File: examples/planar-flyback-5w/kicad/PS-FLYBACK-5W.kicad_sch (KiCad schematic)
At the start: 26 parts, among them J1 18-36 V DC, J2 5 V / 1 A isolated, T1 PLANAR 4:2 / Lm 12uH, U1 LT8302ES8E#PBF

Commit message: Use American Embedded M3 Edge mounting footprints
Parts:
- H1, H2, H3, H4: footprint amemb-MountingHole:MountingHole_3.2mm_M3_ExposedSubstrate -> amemb-MountingHole:MountingHole_3.2mm_M3_ExposedSubstrate_Edge

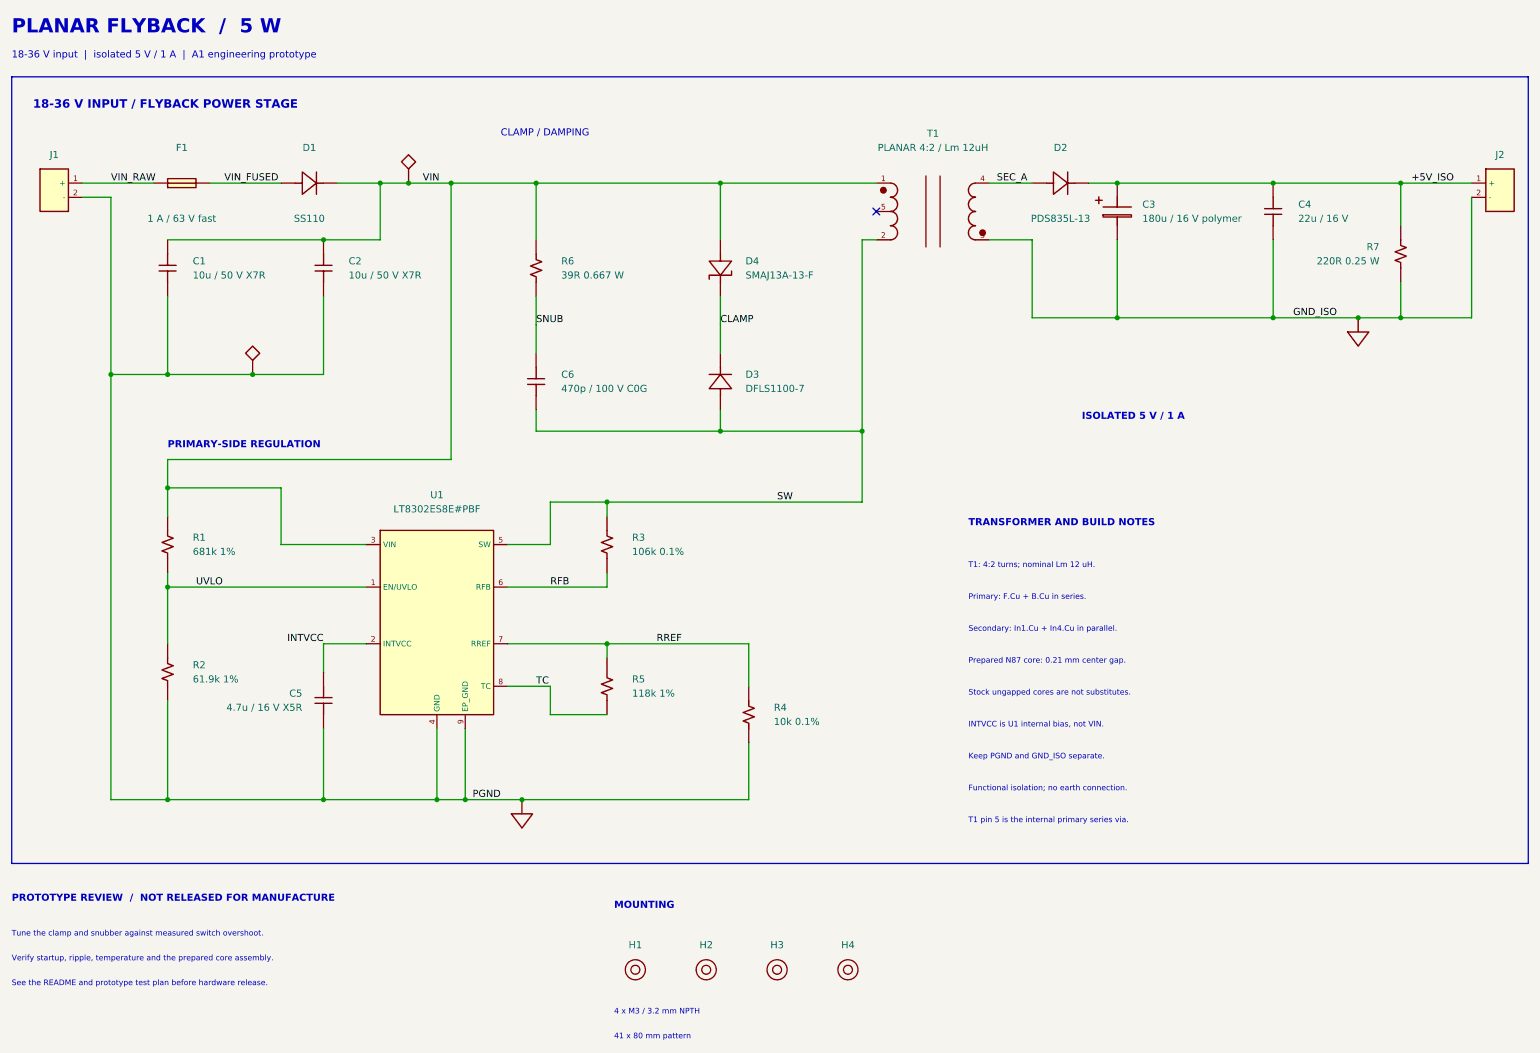
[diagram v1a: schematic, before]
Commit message: Audit flyback components and improve filtering and ground stitching
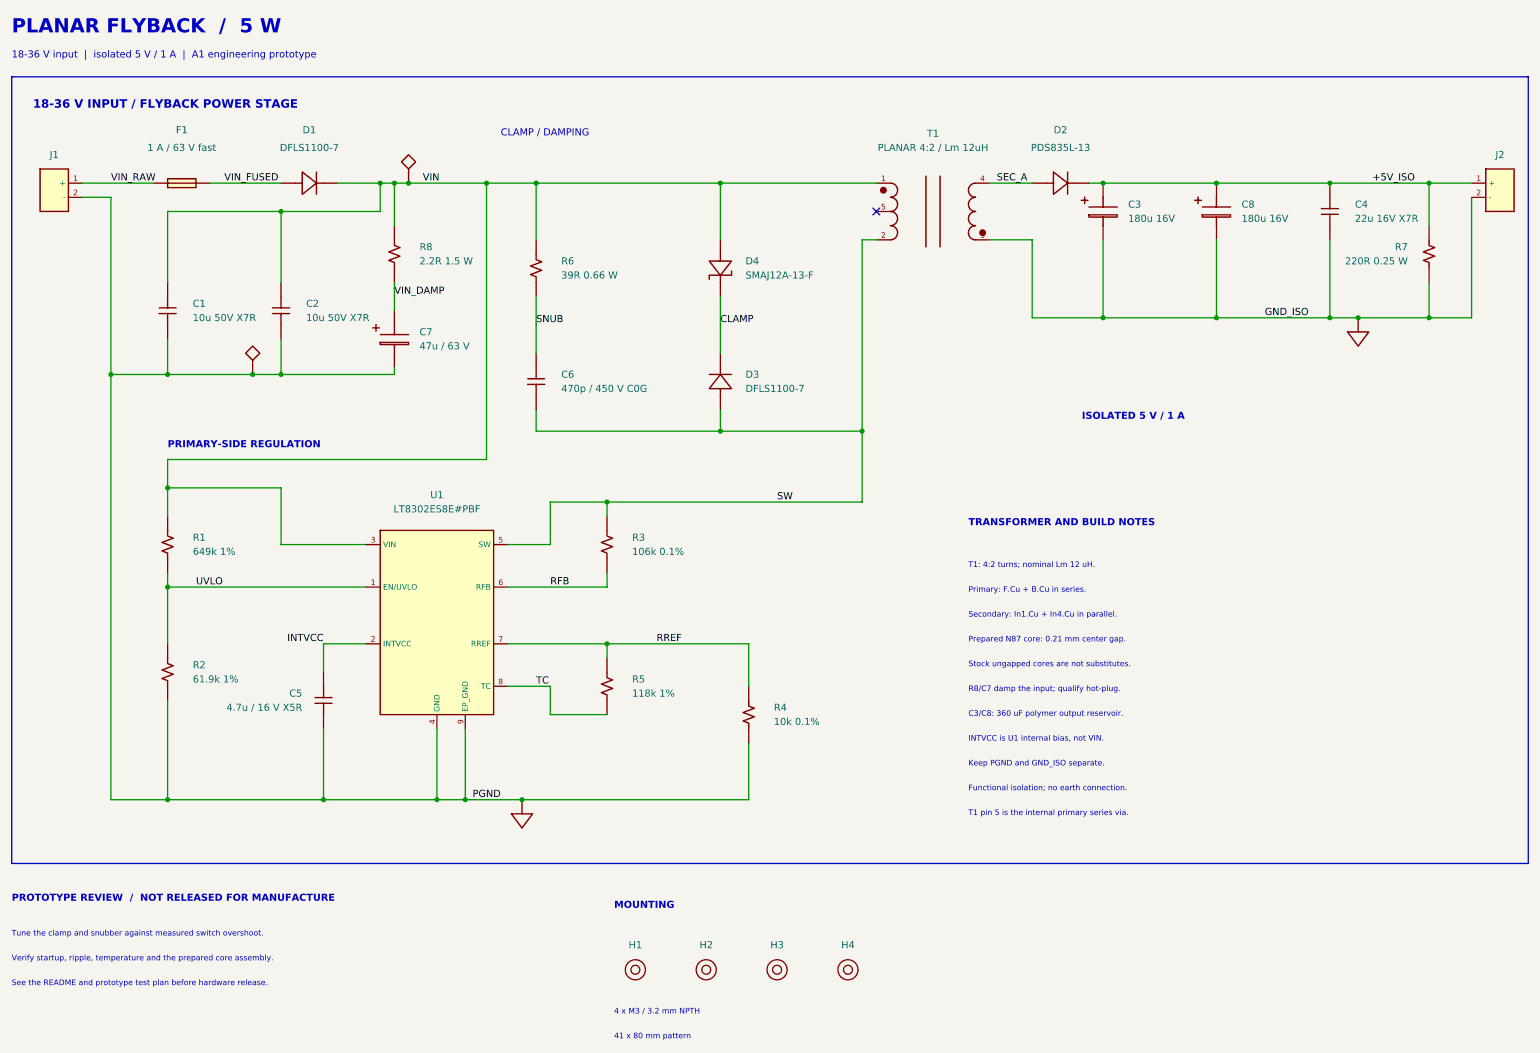
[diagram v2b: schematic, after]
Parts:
- added C7: 47u / 63 V, Flyback:CP_Elec_8x10.5, symbol Flyback:CP
- added C8: 180u 16V, Flyback:CP_Panasonic_C6, symbol Flyback:CP
- added R8: 2.2R 1.5 W, Flyback:R_2512_6332Metric, symbol Flyback:R
- C1, C2: value 10u / 50 V X7R -> 10u 50V X7R
- C3: value 180u / 16 V polymer -> 180u 16V
- C4: value 22u / 16 V -> 22u 16V X7R; LCSC C711059 -> (none); MPN GRM32ER71C226KE18L -> CL32B226KOJNNNE; Manufacturer Murata -> Samsung Electro-Mechanics
- C5: LCSC C19666 -> (none); MPN CL10A475KO8NNNC -> CL10A475KO8NQNC
- C6: value 470p / 100 V C0G -> 470p / 450 V C0G; LCSC C3851794 -> (none); MPN CGA4C2C0G2A471J060AA -> CGA4C4C0G2W471J060AA
- D1: value SS110 -> DFLS1100-7; footprint Flyback:D_SMA -> Flyback:D_PowerDI-123; LCSC C2482 -> C107674; MPN SS110 -> DFLS1100-7; Manufacturer MDD -> Diodes Incorporated
- D4: value SMAJ13A-13-F -> SMAJ12A-13-F; LCSC C110519 -> (none); MPN SMAJ13A-13-F -> SMAJ12A-13-F
- R1: value 681k 1% -> 649k 1%; MPN RC0603FR-07681KL -> RC0603FR-07649KL
- R6: value 39R 0.667 W -> 39R 0.66 W
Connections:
- net +5V_ISO: now also C8.1
- net GND_ISO: now also C8.2
- net PGND: now also C7.2
- net VIN: now also R8.1
- new net VIN_DAMP: C7.1, R8.2
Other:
- note added: "C3/C8: 360 uF polymer output reservoir."
- note added: "R8/C7 damp the input; qualify hot-plug."
- moved on the sheet: C1, C2, C3, C4, R7

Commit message: Move flyback mounting holes to corners for capacitor clearance
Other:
- note added: "41 x 95 mm pattern"
- note removed: "41 x 80 mm pattern"

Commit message: Replace flyback fuse and feedback resistor with stocked JLCPCB parts (#13)
* Replace flyback fuse and correct sourcing scope and 3D model

* Document turnkey blockers and five-board manufacturing budget

* Replace R3 with stocked Vishay precision resistor
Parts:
- C4: LCSC (none) -> C55530
- C5: LCSC (none) -> C377756
- C6: LCSC (none) -> C2172062
- C7: LCSC (none) -> C454353
- D4: LCSC (none) -> C134947
- F1: value 1 A / 63 V fast -> 1 A / 63 V DC fast; footprint Flyback:Fuse_1206_3216Metric -> Flyback:Fuse_Bourns_SF1206F; LCSC C151134 -> C3164649; MPN 0466001.NR -> SF-1206F100-2; Manufacturer Littelfuse -> Bourns
- R1: LCSC (none) -> C245991
- R3: LCSC (none) -> C4185599; MPN RT0603BRD07106KL -> TNPW0603106KBEEN; Manufacturer Yageo -> Vishay
- R6: LCSC (none) -> C4059605
- R8: LCSC (none) -> C4168885

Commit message: Prepare stocked flyback BOM and JLCPCB manufacturing review panel (#14)
* Improve flyback feedback-current margin and prototype clamp budget

* Prepare stocked flyback BOM and JLCPCB assembly review panel

* Normalize generated panel rule file and refresh package integrity
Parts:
- C5: LCSC C377756 -> C77045; MPN CL10A475KO8NQNC -> GRM188R61C475KE11D; Manufacturer Samsung Electro-Mechanics -> Murata
- C6: value 470p / 450 V C0G -> 470p / 100 V C0G; LCSC C2172062 -> C513677; MPN CGA4C4C0G2W471J060AA -> CC0805JRNPO0BN471; Manufacturer TDK -> Yageo
- R3: value 106k 0.1% -> 113k 0.1%; LCSC C4185599 -> C705718; MPN TNPW0603106KBEEN -> RT0603BRD07113KL; Manufacturer Vishay -> Yageo
- R4: value 10k 0.1% -> 10.7k 0.1%; LCSC C95204 -> C861078; MPN RT0603BRD0710KL -> RT0603BRD0710K7L
- R5: value 118k 1% -> 127k 0.1%; LCSC C137804 -> C705722; MPN RC0603FR-07118KL -> RT0603BRD07127KL
- R6: value 39R 0.66 W -> 39R 0.75 W; LCSC C4059605 -> C6683830; MPN ERJ-P08F39R0V -> SR1206FR-7T39RL; Manufacturer Panasonic -> Yageo
- R8: value 2.2R 1.5 W -> 2.2R 2 W; footprint Flyback:R_2512_6332Metric -> Flyback:R_Bourns_CRM2512; LCSC C4168885 -> C840598; MPN CRCW25122R20FKEGHP -> CRM2512-JW-2R2ELF; Manufacturer Vishay -> Bourns
- U1: value LT8302ES8E#PBF -> LT8302IS8E#PBF; LCSC C117331 -> C673679; MPN LT8302ES8E#PBF -> LT8302IS8E#PBF
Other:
- note added: "Tune clamp/snubber: SW-VIN peak <=17.5 V, including overshoot."
- note removed: "Tune the clamp and snubber against measured switch overshoot."

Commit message: Add flyback A2 with stocked factory-gapped ELP22 cores
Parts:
- T1: value PLANAR 4:2 / Lm 12uH -> PLANAR 4:2 / Lm 13.12uH; footprint Flyback:Planar_EELP32_4T_2T -> Flyback:Planar_EELP22_4T_2T; MPN PS-MAG-001 A0 -> PS-MAG-002 A2; Manufacturer Prepared core assembly to drawing -> PCB winding + TDK factory-gapped core pair
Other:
- note added: "18-36 V input | isolated 5 V / 1 A | A2 engineering prototype"
- note added: "2 x B66285G0050X187 (0.05 mm each)."
- note added: "2 x B66286A2000X000 spring clips."
- note added: "T1: 4:2 turns; estimated Lm 13.12 uH."
- note added: "Verify startup, ripple, temperature and the clipped core assembly."
- note removed: "18-36 V input | isolated 5 V / 1 A | A1 engineering prototype"
- note removed: "Prepared N87 core: 0.21 mm center gap."
- note removed: "Stock ungapped cores are not substitutes."
- note removed: "T1: 4:2 turns; nominal Lm 12 uH."
- note removed: "Verify startup, ripple, temperature and the prepared core assembly."
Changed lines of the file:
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@@
 (kicad_sch (version 20250114) (generator "eeschema") (paper "A4")
-(title_block (title "18-36 V to isolated 5 V / 1 A planar flyback") (date "2026-09-29") (rev "A1-development") (company "Planar Studio example"))
+(title_block (title "18-36 V to isolated 5 V / 1 A planar flyback") (date "2026-10-08") (rev "A2-development") (company "Planar Studio example"))

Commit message: Compact flyback A3 and verify TDK clip clearance
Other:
- note added: "18-36 V input | isolated 5 V / 1 A | A3 engineering prototype"
- note added: "35 x 85 mm pattern"
- note removed: "18-36 V input | isolated 5 V / 1 A | A2 engineering prototype"
- note removed: "41 x 95 mm pattern"
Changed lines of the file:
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@@
 (kicad_sch (version 20250114) (generator "eeschema") (paper "A4")
-(title_block (title "18-36 V to isolated 5 V / 1 A planar flyback") (date "2026-10-08") (rev "A2-development") (company "Planar Studio example"))
+(title_block (title "18-36 V to isolated 5 V / 1 A planar flyback") (date "2026-10-08") (rev "A3-development") (company "Planar Studio example"))

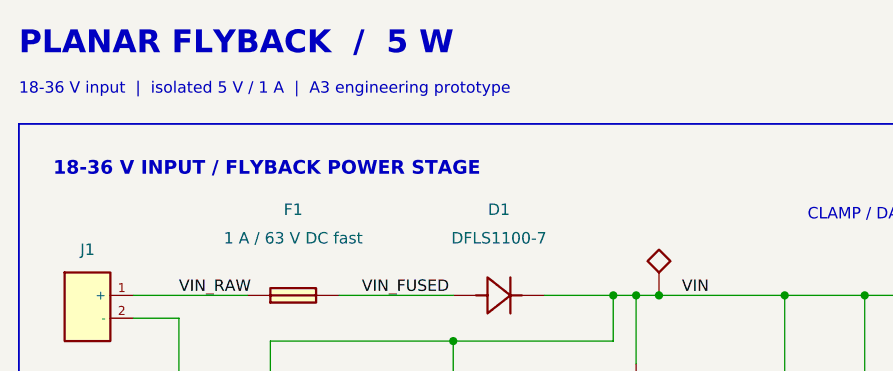
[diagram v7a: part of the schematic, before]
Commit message: Adapt flyback A4 to JLCPCB default 1 oz stack
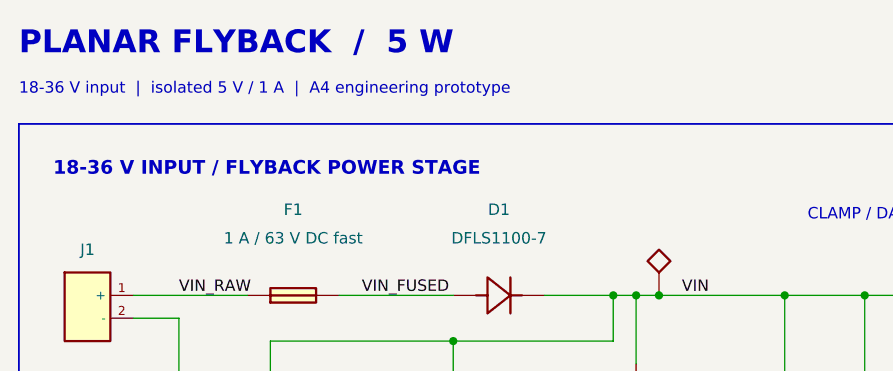
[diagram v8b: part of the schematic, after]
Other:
- note added: "18-36 V input | isolated 5 V / 1 A | A4 engineering prototype"
- note removed: "18-36 V input | isolated 5 V / 1 A | A3 engineering prototype"
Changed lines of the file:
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@@
 (kicad_sch (version 20250114) (generator "eeschema") (paper "A4")
-(title_block (title "18-36 V to isolated 5 V / 1 A planar flyback") (date "2026-10-08") (rev "A3-development") (company "Planar Studio example"))
+(title_block (title "18-36 V to isolated 5 V / 1 A planar flyback") (date "2026-10-08") (rev "A4-development") (company "Planar Studio example"))
